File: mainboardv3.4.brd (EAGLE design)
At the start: 79.7 x 80 mm, 128 parts, among them IC1 LM2596S, IC2 TDA2822D, IC3 MCP2562P, IC4 STM32F103RBT6, IC5 MIC2288YD5, IC6 ULN2003AD, IC7 LM2901, IC8 REG1117, IC9 NC7SZ10P6X, Q1 8MHz

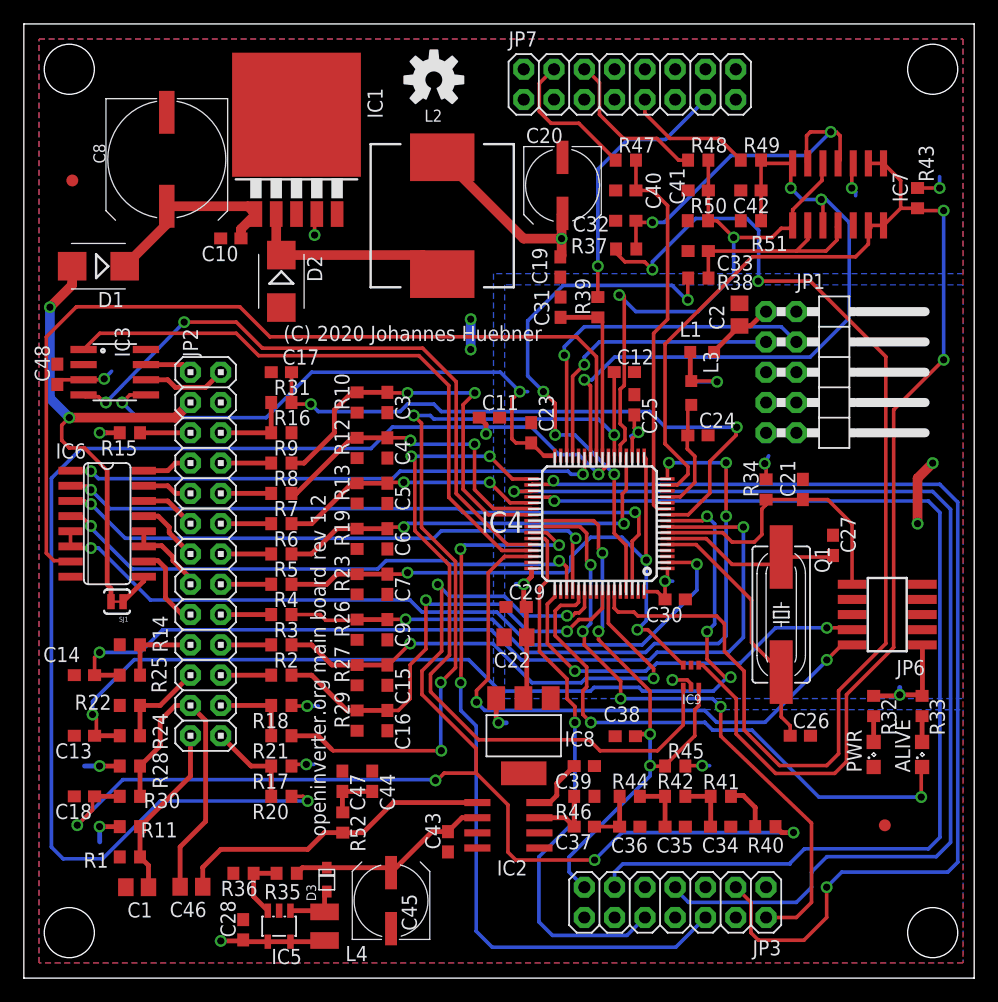
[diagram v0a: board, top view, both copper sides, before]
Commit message: New mainboard v3.4 Using TagConnect for programming Using FET for dcsw output Optimized BOM Added solder bridges for optional resistors
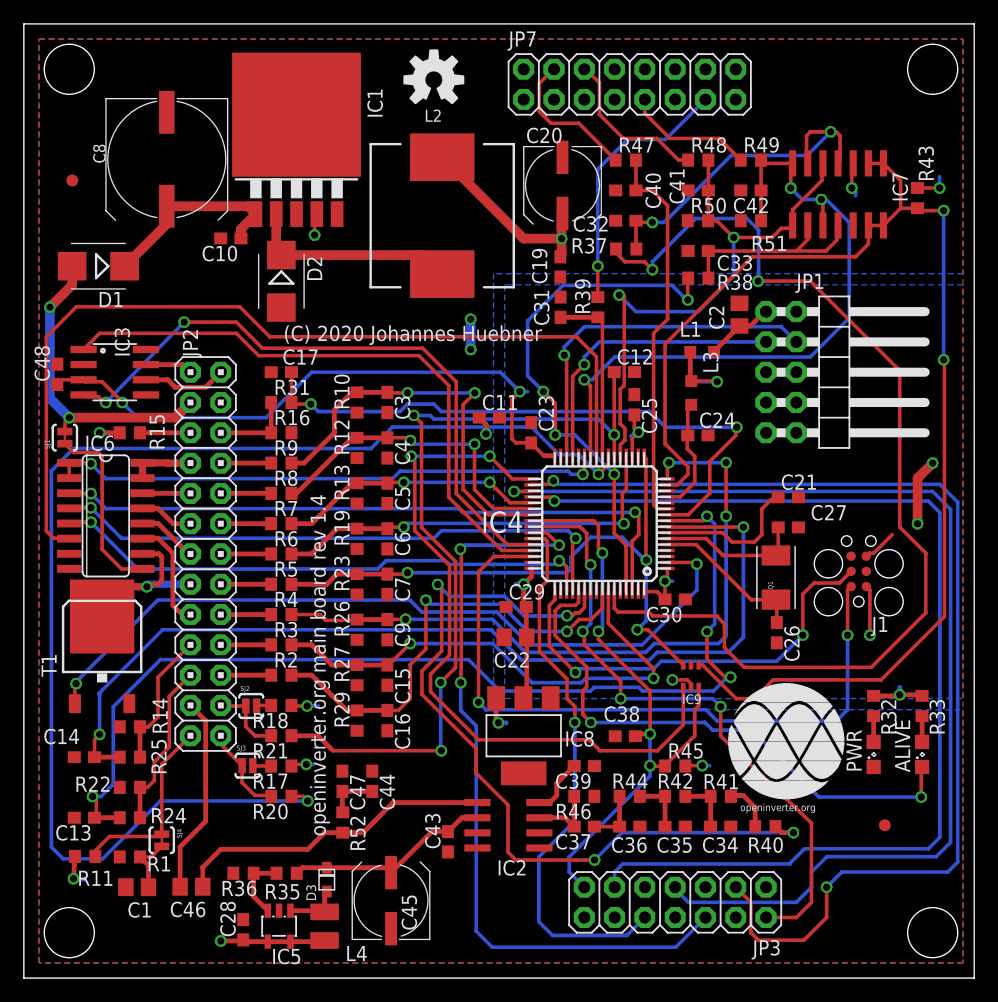
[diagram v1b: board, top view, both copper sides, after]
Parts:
- removed C18: 1nF, rcl:C0603
- removed JP6: (no value), con-leotronics:1365-10
- removed R28: 510, rcl:R0603
- removed R30, R34: 10k, rcl:R0603
- added J1: (no value), tag-connect:TC2030-MCP
- added SJ2, SJ3: SOLDERJUMPERNO, SparkFun-Passives:SJ_2S-NO
- added SJ4: SOLDERJUMPERTRACE, SparkFun-Passives:SJ_2S-TRACE
- added T1: AP9T18GH-HF, transistor-power:D-PAK_TO252AA
- added U$1: OI-LOGO, SparkFun-Aesthetics:OI_LOGO
- IC3: value MCP2562P -> SN65HVD230DR
- Q1: device crystal:HC49UP -> SparkFun-FreqCtrl:CRYSTAL-TXC-7A
- R11: value 120R/510R -> 510R
- moved SJ1 14.4 mm to (3.44, 45.3), turned to 90 degrees
- moved C26 8.86 mm to (63.1, 29.0), turned to 270 degrees
- moved C13 6.88 mm to (5.08, 13.4)
- moved C14 6.88 mm to (5.08, 18.5)
- moved R14 6.88 mm to (8.89, 21.1)
- moved R22 6.88 mm to (8.89, 16.0)
- moved R24 6.88 mm to (8.89, 13.4)
- moved R25 6.88 mm to (8.89, 18.5)
- moved R11 4.51 mm to (5.14, 10.2)
- moved C27 4.04 mm to (64.1, 37.8), turned to 0 degrees
- moved Q1 3.13 mm to (63.1, 33.6), turned to 90 degrees
- moved C21 1.39 mm to (64.1, 40.3), turned to 0 degrees
- moved IC6 0.66 mm to (6.88, 38.8)
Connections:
- new net N$3: R17.2, SJ3.2
- new net N$5: IC4.46, J1.2
- new net N$8: R18.2, SJ2.2
- net ENC_A/S2: now also SJ2.1; no longer R18.2
- net ENC_B/S3: now also SJ3.1; no longer R17.2
- net ENC_Z/R1: no longer R28.2, R30.2
- net GND: now also IC6.7, J1.5, T1.3; no longer C18.2, JP6.3, JP6.5
- net N$2: now also Q1.P$1; no longer Q1.1
- net N$4: now also Q1.P$2; no longer Q1.2
- net N$6: now also IC4.49, J1.4; no longer IC4.46, JP6.2
- net N$9: now also C1.1, R1.2, SJ4.2; no longer IC4.49, JP6.4
- net NRST: no longer JP6.10, R34.1
- net OUT_BRAKE: now also IC6.11; no longer IC6.10
- net OUT_DCSW: now also IC6.10, T1.4; no longer IC6.11, IC6.12
- net OUT_ERR: now also IC6.12; no longer IC6.13
- net OUT_OVTMP: now also IC6.13; no longer IC6.14
- net OUT_PRE: now also IC6.15
- net OUT_TEMP: now also IC6.14; no longer IC6.15
- net PB1/ADC9: now also IC6.2
- net PB9/TIM4_CH4: now also IC6.3; no longer IC6.2
- net PC10: now also IC6.5; no longer IC6.4
- net PC11: now also IC6.4; no longer IC6.3
- net PC13: now also T1.1; no longer IC6.5, IC6.6
- net PC5/ADC15: now also IC6.6; no longer IC6.7
- net PD2/TIM3_ETR: no longer C18.1, R30.1
- net S4/S1: now also SJ4.1; no longer C1.1, R1.2
- net VCC: no longer C48.1, IC3.3, R28.1
- net VCCIO: now also C48.1, IC3.3, J1.1; no longer IC3.5, JP6.1, R34.2
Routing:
- net N$5: track 0.00 -> 58.3 mm, vias 0 -> 2
- net PD2/TIM3_ETR: track 108.8 -> 68.3 mm, vias 6 -> 4
- net N$9: track 32.7 -> 5.03 mm, vias 2 -> 0
- net +12V: track 43.0 -> 26.3 mm
- net N$6: track 50.4 -> 36.5 mm
- net N$1: track 2.81 -> 15.4 mm
- net NRST: track 24.7 -> 12.4 mm
- net ENC_Z/R1: track 26.7 -> 16.6 mm
- net PB7/TIM4_CH2: track 98.3 -> 88.6 mm
- net PA1/TIM2_CH2: track 116.7 -> 107.5 mm
- net N$4: track 21.7 -> 13.0 mm
- net VCC: track 56.2 -> 48.0 mm, vias 13 -> 11
- net OUT_DCSW: track 7.02 -> 13.7 mm, vias 0 -> 1
- net THROTTLE1: track 7.82 -> 14.1 mm
- net PC1/ADC11: track 82.5 -> 88.5 mm
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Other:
- board text added: "openinverter.org main board rev 1.4"
- board text removed: "openinverter.org main board rev 1.2"
